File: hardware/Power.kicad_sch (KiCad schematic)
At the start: 24 parts, among them U2 LD1117S33TR_SOT223, U3 LM2675M-5.0/NOPB

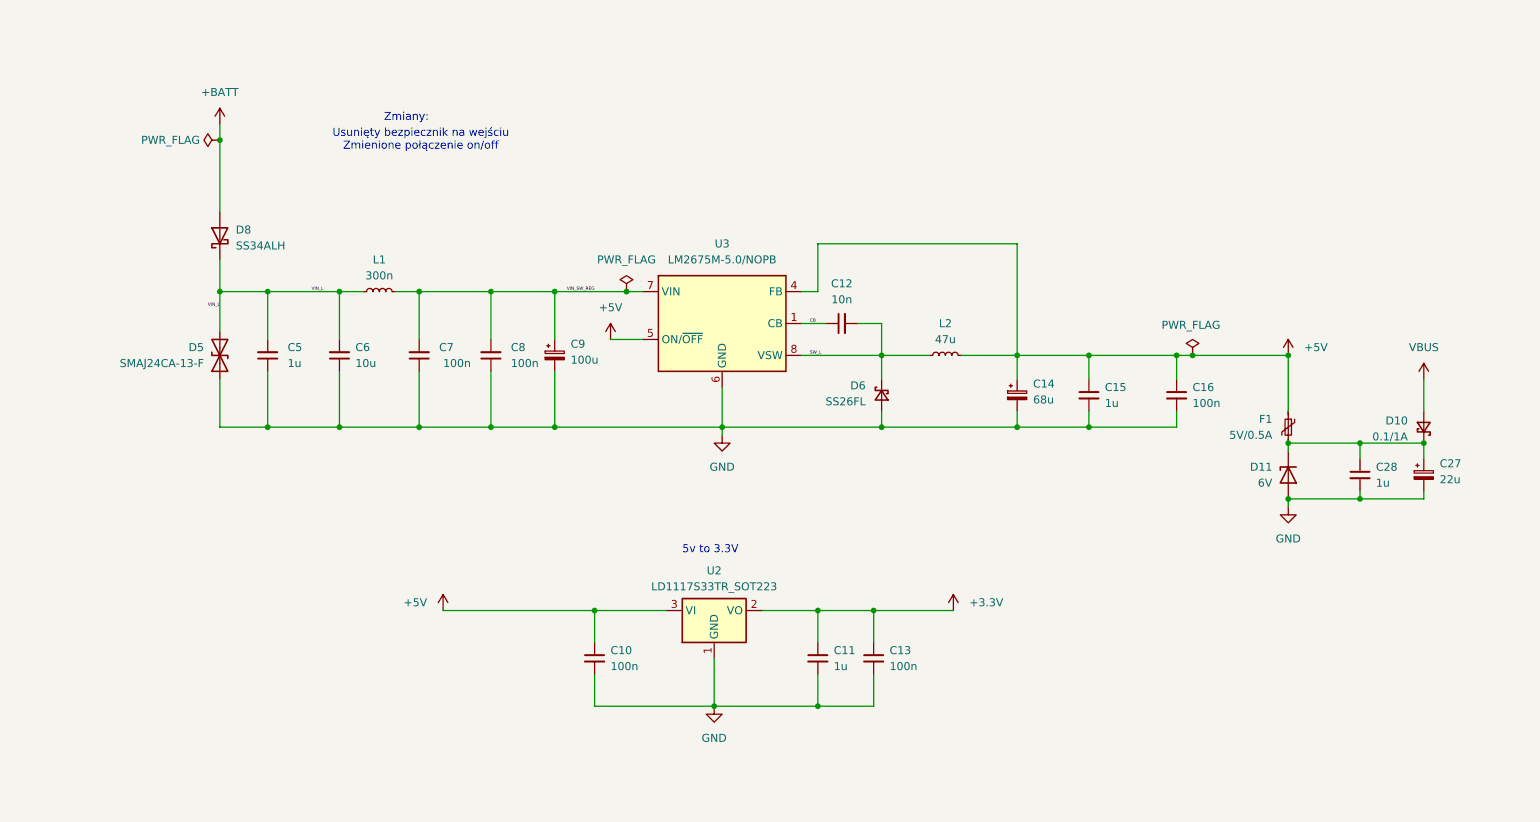
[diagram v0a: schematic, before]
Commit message: cube->cmake port, current calc fix, spi datalength fix, hard-v1.1.0 sync
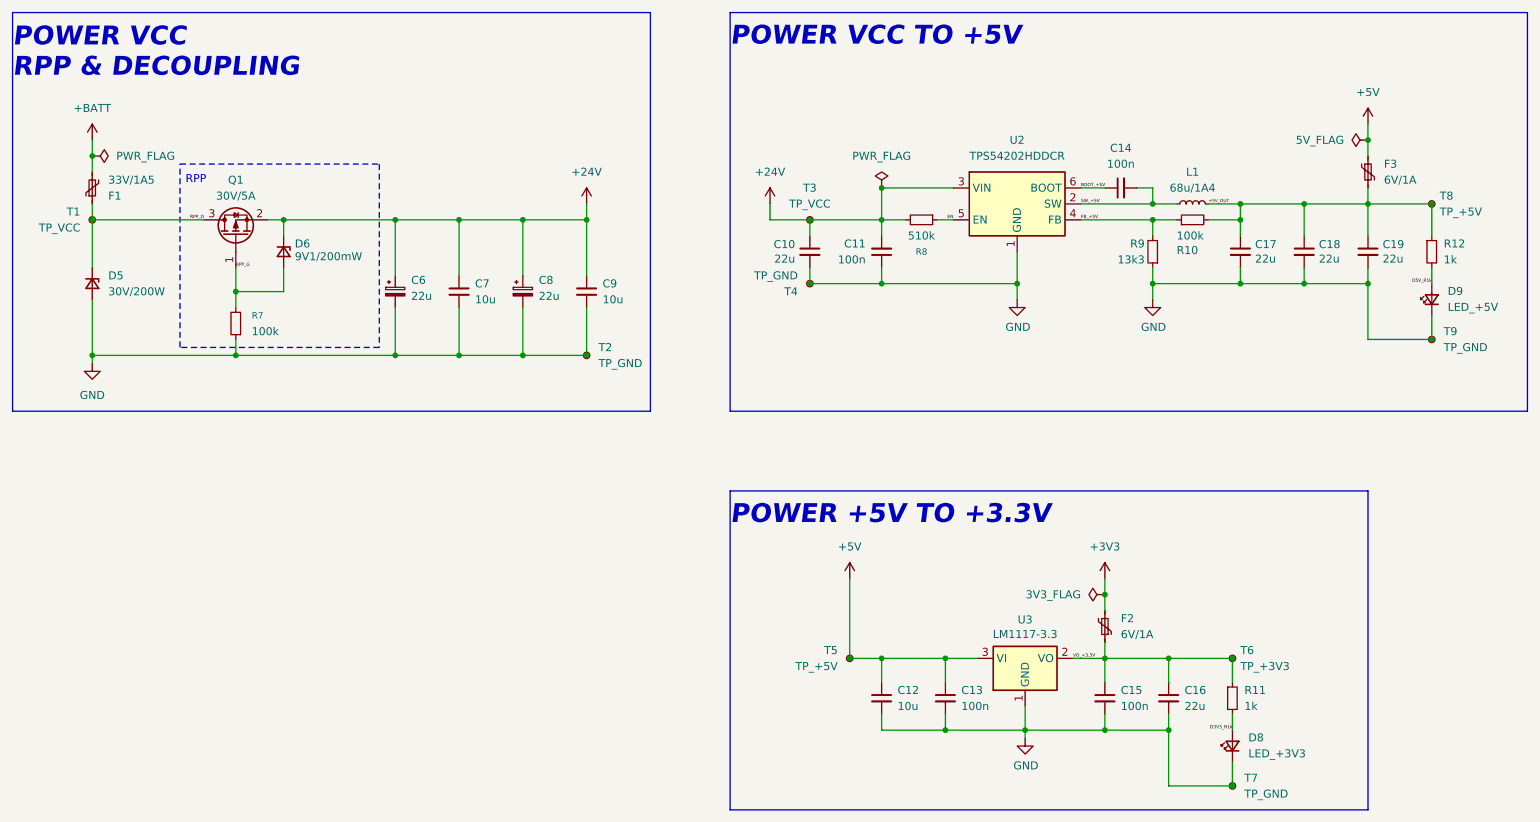
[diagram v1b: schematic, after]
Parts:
- removed C14: 68u, Capacitor_SMD:CP_Elec_6.3x5.4, symbol Device:C_Polarized_Small
- removed C27: 22u, Capacitor_SMD:CP_Elec_4x4.5, symbol Device:C_Polarized_Small
- removed C28: 1u, Capacitor_SMD:C_0603_1608Metric_Pad1.08x0.95mm_HandSolder, symbol Device:C_Small
- removed C5: 1u, Capacitor_SMD:C_0603_1608Metric, symbol Device:C_Small
- removed C6: 10u, Capacitor_SMD:C_0603_1608Metric, symbol Device:C_Small
- removed C8: 100n, Capacitor_SMD:C_0603_1608Metric, symbol Device:C_Small
- removed C9: 100u, Capacitor_SMD:CP_Elec_6.3x7.7, symbol Device:C_Polarized_Small
- removed D10: 0.1/1A, Diode_SMD:D_SMA, symbol Device:D_Schottky_Small
- removed D11: 6V, Diode_SMD:D_SOD-123, symbol Device:D_Zener
- removed D5: SMAJ24CA-13-F, Diode_SMD:D_SMA, symbol Device:D_TVS
- removed D6: SS26FL, Diode_SMD:D_SOD-123, symbol Device:D_Schottky_Small
- removed D8: SS34ALH, Diode_SMD:D_SMA, symbol Diode:1N5822
- removed L2: 47u, Inductor_SMD:L_6.3x6.3_H3, symbol Device:L_Small
- removed U2: LD1117S33TR_SOT223, Package_TO_SOT_SMD:SOT-223-3_TabPin2, symbol Regulator_Linear:LD1117S33TR_SOT223
- removed U3: LM2675M-5.0/NOPB, Package_SO:SOIC-8_3.9x4.9mm_P1.27mm, symbol Regulator_Switching:LM2675M-5
- added C14: 100n, Capacitor_SMD:C_0603_1608Metric_Pad1.08x0.95mm_HandSolder, symbol Device:C_Small
- added C17, C18, C19: 22u, Capacitor_SMD:C_0805_2012Metric_Pad1.18x1.45mm_HandSolder, symbol Device:C_Small
- added C6, C8: 22u, Capacitor_SMD:CP_Elec_5x5.8, symbol Device:C_Polarized_Small
- added C9: 10u, Capacitor_SMD:C_0805_2012Metric_Pad1.18x1.45mm_HandSolder, symbol Device:C_Small
- added D5: 30V/200W, Diode_SMD:D_SOD-123, symbol Device:D_Zener_Small
- added D6: 9V1/200mW, Diode_SMD:D_SOD-323_HandSoldering, symbol Device:D_Zener_Small
- added D8: LED_+3V3, LED_SMD:LED_0603_1608Metric_Pad1.05x0.95mm_HandSolder, symbol Device:LED_Small
- added D9: LED_+5V, LED_SMD:LED_0603_1608Metric_Pad1.05x0.95mm_HandSolder, symbol Device:LED_Small
- added F2, F3: 6V/1A, Fuse:Fuse_0805_2012Metric_Pad1.15x1.40mm_HandSolder, symbol Device:Polyfuse_Small
- added Q1: 30V/5A, Package_TO_SOT_SMD:SOT-23-3, symbol Transistor_FET:Q_PMOS_GSD
- added R10, R7: 100k, Resistor_SMD:R_0603_1608Metric_Pad0.98x0.95mm_HandSolder, symbol Device:R_Small
- added R11, R12: 1k, Resistor_SMD:R_0603_1608Metric_Pad0.98x0.95mm_HandSolder, symbol Device:R_Small
- added R8: 510k, Resistor_SMD:R_0603_1608Metric_Pad0.98x0.95mm_HandSolder, symbol Device:R_Small
- added R9: 13k3, Resistor_SMD:R_0603_1608Metric_Pad0.98x0.95mm_HandSolder, symbol Device:R_Small
- added T1, T3: TP_VCC, TestPoint:TestPoint_Pad_1.0x1.0mm, symbol Connector:TestPoint_Small
- added T2, T4, T7, T9: TP_GND, TestPoint:TestPoint_Pad_1.0x1.0mm, symbol Connector:TestPoint_Small
- added T5, T8: TP_+5V, TestPoint:TestPoint_Pad_1.0x1.0mm, symbol Connector:TestPoint_Small
- added T6: TP_+3V3, TestPoint:TestPoint_Pad_1.0x1.0mm, symbol Connector:TestPoint_Small
- added U2: TPS54202HDDCR, Package_TO_SOT_SMD:SOT-23-6_Handsoldering, symbol Regulator_Switching:TPS54202DDC
- added U3: LM1117-3.3, Package_TO_SOT_SMD:SOT-223-3_TabPin2, symbol Regulator_Linear:LM1117MP-3.3
- C10: value 100n -> 22u; footprint Capacitor_SMD:C_0603_1608Metric -> Capacitor_SMD:C_0805_2012Metric_Pad1.18x1.45mm_HandSolder; Done? (none) -> y; Manufacturer_Name (none) -> MCASH21GCC7684MTCA1J; Manufacturer_Part_Number (none) -> CL21A107MQYNNWE; Mouser Part Number (none) -> 810-C2012X5R1V226MAC; Mouser Price/Stock (none) -> https://www.mouser.pl/ProductDetail/Nichicon/UCM1H220MCL1GS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; m C0603C104K5RAC3121 -> (none)
- C11: value 1u -> 100n; footprint Capacitor_SMD:C_0603_1608Metric -> Capacitor_SMD:C_0603_1608Metric_Pad1.08x0.95mm_HandSolder; Done? (none) -> y; Manufacturer_Name (none) -> --; Manufacturer_Part_Number (none) -> C0603C104J3RACTU; Mouser Part Number (none) -> 81-GCJ188R71H104KA2D; Mouser Price/Stock (none) -> https://www.mouser.pl/ProductDetail/Murata-Electronics/GCJ1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; m CL10B105KB8NQNC -> (none)
- C12: value 10n -> 10u; footprint Capacitor_SMD:C_0603_1608Metric -> Capacitor_SMD:C_0805_2012Metric_Pad1.18x1.45mm_HandSolder; Done? (none) -> y; Mouser Part Number (none) -> 81-GRM21BR61H106KE3L; Mouser Price/Stock (none) -> https://www.mouser.pl/ProductDetail/Murata-Electronics/GRM2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; m C0603C103J5RAC7411 -> (none)
- C13: footprint Capacitor_SMD:C_0603_1608Metric -> Capacitor_SMD:C_0603_1608Metric_Pad1.08x0.95mm_HandSolder; Done? (none) -> y; Mouser Part Number (none) -> 81-GCJ188R71H104KA2D; Mouser Price/Stock (none) -> https://www.mouser.pl/ProductDetail/Murata-Electronics/GCJ1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; m C0603C104K5RAC3121 -> (none)
- C15: value 1u -> 100n; footprint Capacitor_SMD:C_0603_1608Metric -> Capacitor_SMD:C_0603_1608Metric_Pad1.08x0.95mm_HandSolder; Done? (none) -> y; Mouser Part Number (none) -> 81-GCJ188R71H104KA2D; Mouser Price/Stock (none) -> https://www.mouser.pl/ProductDetail/Murata-Electronics/GCJ1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; m CL10B105KB8NQNC -> (none)
- C16: value 100n -> 22u; footprint Capacitor_SMD:C_0603_1608Metric -> Capacitor_SMD:C_0805_2012Metric_Pad1.18x1.45mm_HandSolder; Done? (none) -> y; Mouser Part Number (none) -> 810-C2012X5R1V226MAC; Mouser Price/Stock (none) -> https://www.mouser.pl/ProductDetail/TDK/C2012X5R1V226M125AC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; m C0603C104K5RAC3121 -> (none)
- C7: value 100n -> 10u; footprint Capacitor_SMD:C_0603_1608Metric -> Capacitor_SMD:C_0805_2012Metric_Pad1.18x1.45mm_HandSolder; Done? (none) -> y; Mouser Part Number (none) -> 81-GRM21BR61H106KE3L; Mouser Price/Stock (none) -> https://www.mouser.pl/ProductDetail/Murata-Electronics/GRM2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; m C0603C104K5RAC3121 -> (none)
- F1: value 5V/0.5A -> 33V/1A5; footprint Fuse:Fuse_1206_3216Metric_Pad1.42x1.75mm_HandSolder -> Fuse:Fuse_2920_7451Metric_Pad2.10x5.45mm_HandSolder; Done? (none) -> y; Mouser https://www.mouser.pl/ProductDetail/Eaton-Electronics/PTS12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 -> (none); Mouser Part Number (none) -> 530-0ZCF0075AF2C; Mouser Price/Stock (none) -> https://eu.mouser.com/ProductDetail/Bel-Fuse/0ZCF0075AF2C?q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
- L1: value 300n -> 68u/1A4; footprint Inductor_SMD:L_0603_1608Metric -> Inductor_SMD:L_TDK_VLS6045EX_VLS6045AF; Done? (none) -> y; Height (none) -> 4.5mm; Manufacturer_Name (none) -> TDK; Manufacturer_Part_Number (none) -> VLS6045EX-680M; Mouser Part Number (none) -> 810-VLS6045EX-680M; Mouser Price/Stock (none) -> https://www.mouser.pl/ProductDetail/TDK/VLS6045EX-680M?qs=o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; m ASMPL-0603-R33M-T -> (none); mouser https://www.mouser.pl/ProductDetail/ABRACON/ASMPL-0603-R33M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 -> (none)
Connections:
- net CB is gone; now on net +5V: C12.1
- net SW_L is gone; now on net GND: C12.2
- net +5V: now also C13.1, F3.1, T5.1, U3.3 (VI); no longer C10.1, C15.1, C16.1, F1.1
- net +BATT: now also F1.2
- net GND: now also C11.1, C7.2, C17.2, C18.2, C19.2, C6.2, C8.2, C9.2, D5.2 (A), D8.1 (K), D9.1 (K), R7.1, R9.1, T2.1, T4.1, T7.1, T9.1, U2.1 (GND), U3.1 (GND); no longer C11.2, C7.1
- removed net +3.3V: C11.1, C13.1
- net VIN_L renamed SW_+5V
- net SW_+5V: now also C14.2, U2.2 (SW)
- net VIN_SW_REG renamed +5V_OUT
- net +5V_OUT: now also C17.1, C18.1, C19.1, F3.2, R10.2, R12.1, T8.1; no longer C7.2
- new net +24V: C10.1, C11.2, C6.1, C7.1, C8.1, C9.1, D6.1 (K), Q1.2 (S), R8.2, T3.1, U2.3 (VIN)
- new net +3V3: F2.2
- new net BOOT_+5V: C14.1, U2.6 (BOOT)
- new net D3V3_R1k: D8.2 (A), R11.2
- new net D5V_R1k: D9.2 (A), R12.2
- new net EN: R8.1, U2.5 (EN)
- new net FB_+5V: R10.1, R9.2, U2.4 (FB)
- new net RPP_D: D5.1 (K), F1.1, Q1.3 (D), T1.1
- new net RPP_G: D6.2 (A), Q1.1 (G), R7.2
- new net VO_+3.3V: C15.1, C16.1, F2.1, R11.1, T6.1, U3.2 (VO)
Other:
- note added: "POWER +5V TO +3.3V"
- note added: "POWER VCC RPP & DECOUPLING"
- note added: "POWER VCC TO +5V"
- note added: "RPP"
- note removed: "5v to 3.3V"
- note removed: "Usunięty bezpiecznik na wejściu Zmienione połączenie on/off"
- note removed: "Zmiany:"
- company: (none) -> Authors: Grzegorz Potocki Jędrzej Kasprzyk
- title: (none) -> PDUv3
